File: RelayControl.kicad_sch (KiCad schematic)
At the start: 20 parts, among them U15 TIP29A, U16 TIP29A, U17 TIP29A, U18 TIP29A, U19 INA226, U20 INA226, U21 INA226, U22 INA226

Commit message: Solved errors
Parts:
- removed R39, R40, R41, R42: 50m, Resistor_SMD:R_2512_6332Metric_Pad1.40x3.35mm_HandSolder, symbol Device:R
- removed U19, U20, U21, U22: INA226, Package_SO:VSSOP-10_3x3mm_P0.5mm, symbol Sensor_Energy:INA226
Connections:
- no-connect marks 4 -> 0

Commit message: New PCB Changes
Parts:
- removed U15, U16, U17, U18: TIP29A, TO-220AB_ONS_STM, symbol Mnalib:TIP29A
- added U14, U15, U16, U17: TIP29A, Library:TO-220AB_ONS, symbol TIP 29A:TIP29A
- D12, D13, D14, D15: footprint (none) -> Diode_SMD:D_0805_2012Metric_Pad1.15x1.40mm_HandSolder
- R36, R37, R38: footprint (none) -> Resistor_SMD:R_0805_2012Metric
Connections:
- net +24V: now also U14.2 (COLLECTOR), U15.2 (COLLECTOR), U16.2 (COLLECTOR), U17.3 (EMITTER)
- net K1OUT: now also U14.3 (EMITTER)
- net K2OUT: now also U15.3 (EMITTER)
- net K3OUT: now also U16.3 (EMITTER)
- net K4OUT: now also U17.2 (COLLECTOR)
- net at R36.2: now also U15.1 (BASE)
- net at R38.2: now also U17.1 (BASE)
- net at R37.2: now also U16.1 (BASE)
- net at R35.2: now also U14.1 (BASE)
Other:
- moved on the sheet: R35

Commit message: FInal Changes in Schgematic
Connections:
- net +24V renamed +24
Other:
- moved on the sheet: D12, D13, D14, D15, R35, R36, R37, R38, U14, U15, U16, U17

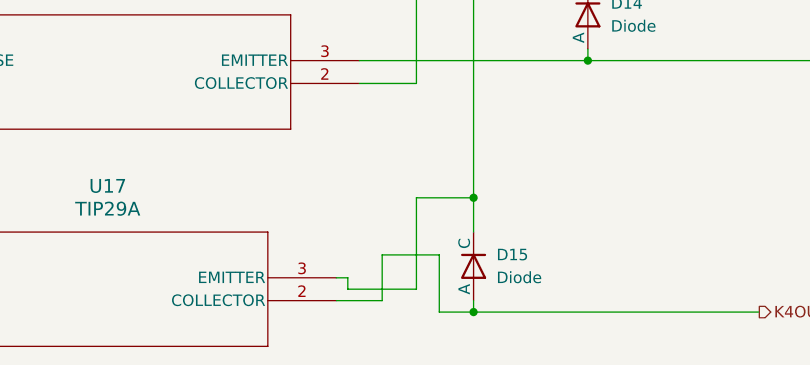
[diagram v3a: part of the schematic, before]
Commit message: Used Zones and Net
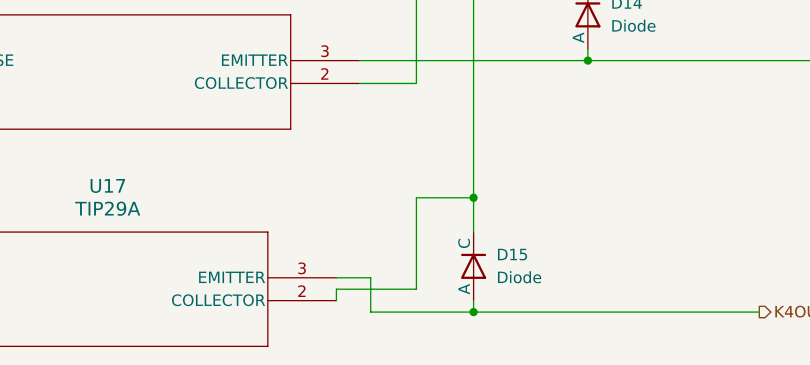
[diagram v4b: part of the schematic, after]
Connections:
- net +24: now also U17.2 (COLLECTOR); no longer U17.3 (EMITTER)
- net K4OUT: now also U17.3 (EMITTER); no longer U17.2 (COLLECTOR)
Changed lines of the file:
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@@
 	(wire
 		(pts
-			(xy 156.21 115.57) (xy 160.02 115.57)
+			(xy 148.59 115.57) (xy 160.02 115.57)
+		)
+		(stroke
+			(width 0)
+			(type default)
+		)
+	)
+	(wire
+		(pts
+			(xy 148.59 111.76) (xy 148.59 115.57)
 		)
 		(stroke
@@
 	(wire
 		(pts
+			(xy 144.78 113.03) (xy 144.78 114.3)
+		)
+		(stroke
+			(width 0)
+			(type default)
+		)
+	)
+	(wire
+		(pts
 			(xy 167.64 35.56) (xy 167.64 33.02)
 		)
@@
 	(wire
 		(pts
-			(xy 146.05 113.03) (xy 146.05 111.76)
-		)
-		(stroke
-			(width 0)
-			(type default)
-		)
-	)
-	(wire
-		(pts
 			(xy 154.94 31.75) (xy 160.02 31.75)
 		)
@@
 	(wire
 		(pts
-			(xy 144.78 111.76) (xy 146.05 111.76)
+			(xy 144.78 111.76) (xy 148.59 111.76)
 		)
 		(stroke
@@
 	(wire
 		(pts
+			(xy 153.67 113.03) (xy 144.78 113.03)
+		)
+		(stroke
+			(width 0)
+			(type default)
+		)
+	)
+	(wire
+		(pts
 			(xy 160.02 57.15) (xy 172.72 57.15)
 		)
@@
 	(wire
 		(pts
-			(xy 149.86 109.22) (xy 149.86 114.3)
-		)
-		(stroke
-			(width 0)
-			(type default)
-		)
-	)
-	(wire
-		(pts
 			(xy 160.02 78.74) (xy 172.72 78.74)
 		)
@@
 	(wire
 		(pts
-			(xy 156.21 109.22) (xy 156.21 115.57)
-		)
-		(stroke
-			(width 0)
-			(type default)
-		)
-	)
-	(wire
-		(pts
 			(xy 167.64 33.02) (xy 160.02 33.02)
 		)
@@
 	(wire
 		(pts
-			(xy 149.86 109.22) (xy 156.21 109.22)
-		)
-		(stroke
-			(width 0)
-			(type default)
-		)
-	)
-	(wire
-		(pts
 			(xy 77.47 111.76) (xy 86.36 111.76)
 		)
@@
 	(wire
 		(pts
-			(xy 144.78 114.3) (xy 149.86 114.3)
-		)
-		(stroke
-			(width 0)
-			(type default)
-		)
-	)
-	(wire
-		(pts
 			(xy 152.4 60.96) (xy 156.21 60.96)
 		)
@@
 		)
 		(stroke
-			(width 0)
-			(type default)
-		)
-	)
-	(wire
-		(pts
-			(xy 153.67 113.03) (xy 146.05 113.03)
-		)
-		(stroke
